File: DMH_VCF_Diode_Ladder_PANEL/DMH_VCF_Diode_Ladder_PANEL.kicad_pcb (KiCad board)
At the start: 2 copper layers, 100 x 200 mm, 20 parts, among them J0 Panel_GND_Solder_Wire_Pad

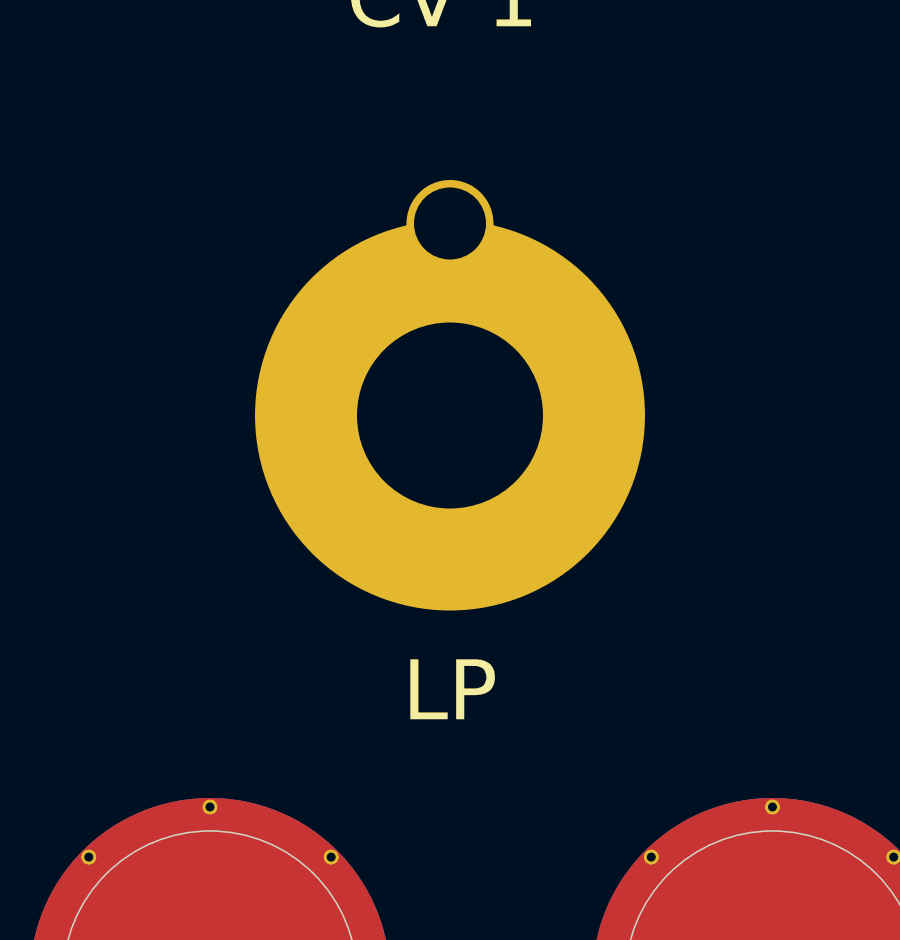
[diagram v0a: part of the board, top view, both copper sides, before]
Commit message: Component placement in progress
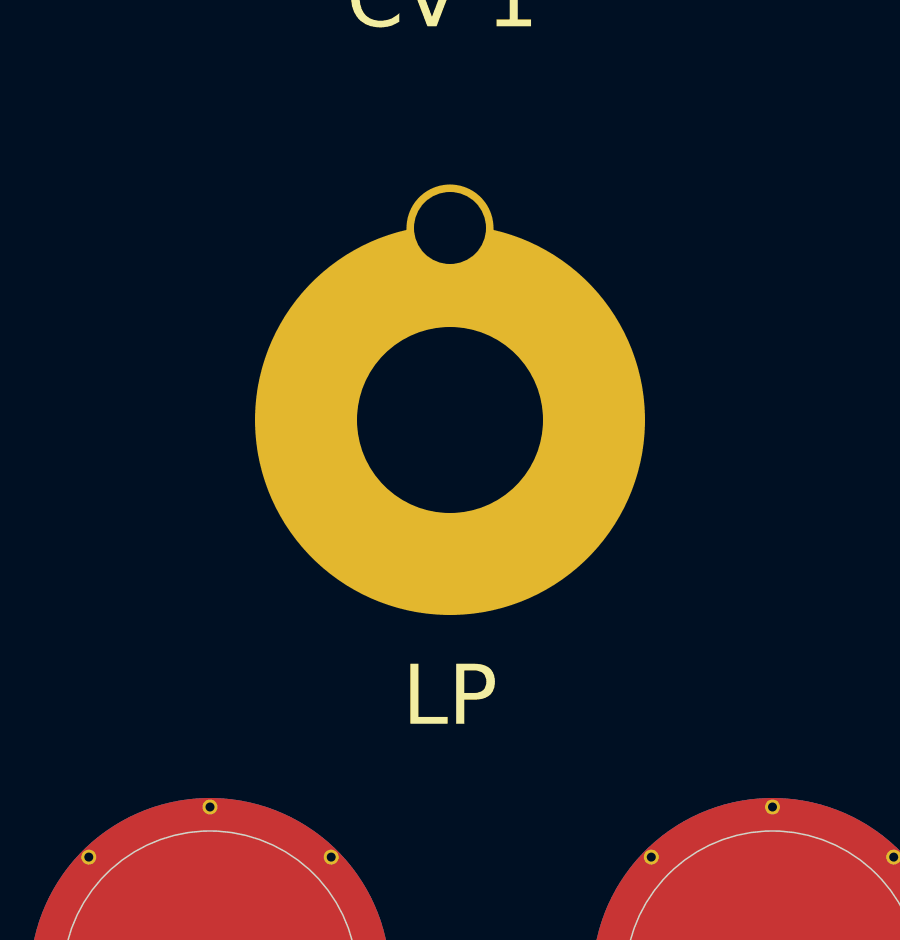
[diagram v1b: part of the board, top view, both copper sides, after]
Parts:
- moved H14 0.15 mm to (70.5, 190.2)
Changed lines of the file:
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@@
 	(footprint "SynthStuff:Toggle_Switch_Cutout"
 		(layer "F.Cu")
-		(at 70.5 190)
+		(at 70.5 190.15)
 		(property "Reference" "H14"
 			(at 0 -4 0)
@@
 				(polygon
 					(pts
-						(xy 70.351989 200.03) (xy 70.351989 199.54591) (xy 69.038451 199.54591) (xy 68.94125 199.53182)
-						(xy 68.878189 199.451526) (xy 68.870412 199.364682) (xy 68.870412 198.122951) (xy 68.360921 198.122951)
-						(xy 68.360921 199.413042) (xy 68.365047 199.523638) (xy 68.377958 199.623255) (xy 68.41022 199.73904)
-						(xy 68.461415 199.835399) (xy 68.533439 199.912383) (xy 68.628186 199.970045) (xy 68.747551 200.008435)
-						(xy 68.85437 200.024612) (xy 68.976902 200.03)
+						(xy 70.351989 200.18) (xy 70.351989 199.69591) (xy 69.038451 199.69591) (xy 68.94125 199.68182)
+						(xy 68.878189 199.601526) (xy 68.870412 199.514682) (xy 68.870412 198.272951) (xy 68.360921 198.272951)
+						(xy 68.360921 199.563042) (xy 68.365047 199.673638) (xy 68.377958 199.773255) (xy 68.41022 199.88904)
+						(xy 68.461415 199.985399) (xy 68.533439 200.062383) (xy 68.628186 200.120045) (xy 68.747551 200.158435)
+						(xy 68.85437 200.174612) (xy 68.976902 200.18)
 					)
 				)
 				(polygon
 					(pts
-						(xy 72.020964 198.126577) (xy 72.12988 198.140919) (xy 72.226763 198.165493) (xy 72.328699 198.207482)
-						(xy 72.416814 198.261939) (xy 72.493022 198.327627) (xy 72.517116 198.352857) (xy 72.581483 198.435231)
-						(xy 72.633229 198.526518) (xy 72.671386 198.625288) (xy 72.694988 198.730112) (xy 72.703071 198.83956)
-						(xy 72.700224 198.904337) (xy 72.682046 199.014098) (xy 72.648125 199.11799) (xy 72.599688 199.21451)
-						(xy 72.537962 199.302156) (xy 72.513024 199.330457) (xy 72.428702 199.407119) (xy 72.346783 199.460535)
-						(xy 72.253427 199.50329) (xy 72.14784 199.534309) (xy 72.029227 199.55252) (xy 71.924424 199.557145)
-						(xy 71.053943 199.557145) (xy 71.053943 200.03) (xy 70.546895 200.03) (xy 70.546895 198.66517)
-						(xy 71.053943 198.66517) (xy 71.053943 199.092107) (xy 71.93566 199.092107) (xy 71.975597 199.090503)
-						(xy 72.077997 199.064427) (xy 72.154501 198.999295) (xy 72.179014 198.957389) (xy 72.198953 198.860076)
-						(xy 72.193165 198.803113) (xy 72.15157 198.711577) (xy 72.125422 198.684143) (xy 72.033481 198.636226)
-						(xy 71.93566 198.624626) (xy 71.090091 198.624626) (xy 71.053943 198.66517) (xy 70.546895 198.66517)
-						(xy 70.546895 198.240676) (xy 70.574285 198.156306) (xy 70.669993 198.122951) (xy 71.924424 198.122951)
+						(xy 72.020964 198.276577) (xy 72.12988 198.290919) (xy 72.226763 198.315493) (xy 72.328699 198.357482)
+						(xy 72.416814 198.411939) (xy 72.493022 198.477627) (xy 72.517116 198.502857) (xy 72.581483 198.585231)
+						(xy 72.633229 198.676518) (xy 72.671386 198.775288) (xy 72.694988 198.880112) (xy 72.703071 198.98956)
+						(xy 72.700224 199.054337) (xy 72.682046 199.164098) (xy 72.648125 199.26799) (xy 72.599688 199.36451)
+						(xy 72.537962 199.452156) (xy 72.513024 199.480457) (xy 72.428702 199.557119) (xy 72.346783 199.610535)
+						(xy 72.253427 199.65329) (xy 72.14784 199.684309) (xy 72.029227 199.70252) (xy 71.924424 199.707145)
+						(xy 71.053943 199.707145) (xy 71.053943 200.18) (xy 70.546895 200.18) (xy 70.546895 198.81517)
+						(xy 71.053943 198.81517) (xy 71.053943 199.242107) (xy 71.93566 199.242107) (xy 71.975597 199.240503)
+						(xy 72.077997 199.214427) (xy 72.154501 199.149295) (xy 72.179014 199.107389) (xy 72.198953 199.010076)
+						(xy 72.193165 198.953113) (xy 72.15157 198.861577) (xy 72.125422 198.834143) (xy 72.033481 198.786226)
+						(xy 71.93566 198.774626) (xy 71.090091 198.774626) (xy 71.053943 198.81517) (xy 70.546895 198.81517)
+						(xy 70.546895 198.390676) (xy 70.574285 198.306306) (xy 70.669993 198.272951) (xy 71.924424 198.272951)
 					)
 				)
